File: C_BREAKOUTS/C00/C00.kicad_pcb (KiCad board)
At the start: 2 copper layers, 88.9 x 38.1 mm, 42 parts, among them J0 Conn_01x01_Male, J1 Conn_01x01_Male, J2 Conn_01x01_Male, J3 Conn_01x01_Male, J6 Conn_01x06_Female, J7 Conn_01x06_Female

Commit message: some comfort improvement
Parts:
- moved J0 20.3 mm to (49.2, 28.9)
- moved J1 20.3 mm to (49.2, 49.2)
- moved HZ3 1.30 mm to (91.3, 51.5)
- moved J7 0.40 mm to (97.0, 30.3)
- moved HZ0 0.40 mm to (23.4, 26.6)
- moved HZ1 0.40 mm to (23.4, 51.5)
- moved J6 0.30 mm to (104.9, 47.8)
- moved HZ2 0.30 mm to (92.3, 26.6)
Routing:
- net Net-(J6-Pad6): track 16.0 -> 0.00 mm
- net Net-(J6-Pad5): track 16.0 -> 0.00 mm
- net Net-(J6-Pad4): track 16.0 -> 0.00 mm
- net Net-(J6-Pad3): track 16.0 -> 0.00 mm
- net Net-(J6-Pad2): track 16.0 -> 0.00 mm
- net Net-(J6-Pad1): track 16.0 -> 0.00 mm
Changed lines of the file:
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@@
     (thickness 1.6)
     (drawings 8)
-    (tracks 15)
+    (tracks 0)
     (zones 0)
     (modules 42)
@@
   )
   (module TerminalBlock_4Ucon:TerminalBlock_4Ucon_1x06_P3.50mm_Horizontal (layer F.Cu)
-    (at 96.6 30.3 270)
+    (at 97 30.3 270)
     (descr "Terminal Block 4Ucon ItemNo. 19964, 6 pins, pitch 3.5mm, size 21.7x7mm^2, drill diamater 1.2mm, pad diameter 2.4mm, see http://www.4uconnector.com/online/object/4udrawing/19964.pdf, script-generated using https://github.com/pointhi/kicad-footprint-generator/scripts/TerminalBlock_4Ucon")
     (tags "THT Terminal Block 4Ucon ItemNo. 19964 pitch 3.5mm size 21.7x7mm^2 drill 1.2mm pad 2.4mm")
@@
   )
   (module TerminalBlock_4Ucon:TerminalBlock_4Ucon_1x06_P3.50mm_Horizontal (layer F.Cu)
-    (at 104.6 47.8 90)
+    (at 104.9 47.8 90)
     (descr "Terminal Block 4Ucon ItemNo. 19964, 6 pins, pitch 3.5mm, size 21.7x7mm^2, drill diamater 1.2mm, pad diameter 2.4mm, see http://www.4uconnector.com/online/object/4udrawing/19964.pdf, script-generated using https://github.com/pointhi/kicad-footprint-generator/scripts/TerminalBlock_4Ucon")
     (tags "THT Terminal Block 4Ucon ItemNo. 19964 pitch 3.5mm size 21.7x7mm^2 drill 1.2mm pad 2.4mm")
@@
   )
   (module Connector_Wire:SolderWirePad_1x01_Drill1mm (layer F.Cu)
-    (at 28.89 49.21)
+    (at 49.21 49.21)
     (descr "Wire solder connection")
     (tags connector)
@@
   )
   (module Connector_Wire:SolderWirePad_1x01_Drill1mm (layer F.Cu)
-    (at 28.89 28.89)
+    (at 49.21 28.89)
     (descr "Wire solder connection")
     (tags connector)
@@
   )
   (module MountingHole:MountingHole_3mm (layer F.Cu)
-    (at 92.56 51.55)
+    (at 91.26 51.55)
     (descr "Mounting Hole 3mm, no annular")
     (tags "mounting hole 3mm no annular")
@@
   )
   (module MountingHole:MountingHole_3mm (layer F.Cu)
-    (at 92.56 26.55)
+    (at 92.26 26.55)
     (descr "Mounting Hole 3mm, no annular")
     (tags "mounting hole 3mm no annular")
@@
   )
   (module MountingHole:MountingHole_3mm (layer F.Cu)
-    (at 23.81 51.55)
+    (at 23.41 51.55)
     (descr "Mounting Hole 3mm, no annular")
     (tags "mounting hole 3mm no annular")
@@
   )
   (module MountingHole:MountingHole_3mm (layer F.Cu)
-    (at 23.81 26.55)
+    (at 23.41 26.55)
     (descr "Mounting Hole 3mm, no annular")
     (tags "mounting hole 3mm no annular")
@@
     (effects (font (size 1.5 1.5) (thickness 0.3)))
   )
-  (gr_text C00_BREAKOUT (at 39.5224 29.0322 180) (layer B.SilkS)
+  (gr_text C00_BREAKOUT (at 37.5224 29.0322 180) (layer B.SilkS)
     (effects (font (size 1.5 1.5) (thickness 0.15)) (justify mirror))
   )
-  (gr_text C00_BREAKOUT (at 40.1574 49.3776) (layer F.SilkS)
+  (gr_text C00_BREAKOUT (at 38.1574 49.3776) (layer F.SilkS)
     (effects (font (size 1.5 1.5) (thickness 0.15)))
   )
@@
   (gr_line (start 20 20) (end 108.9 20) (layer Edge.Cuts) (width 0.05))
   (gr_line (start 20 20) (end 20 58.1) (layer Edge.Cuts) (width 0.05))
-  (segment (start 96.6 30.3) (end 104.6 30.3) (width 0.75) (layer F.Cu) (net 2))
-  (segment (start 96.6 30.3) (end 104.6 30.3) (width 0.75) (layer B.Cu) (net 2))
-  (segment (start 96.6 33.8) (end 104.6 33.8) (width 0.75) (layer F.Cu) (net 3))
-  (segment (start 96.6 33.8) (end 104.6 33.8) (width 0.75) (layer B.Cu) (net 3))
-  (segment (start 96.6 37.3) (end 104.6 37.3) (width 0.75) (layer F.Cu) (net 4))
-  (segment (start 98.297056 37.3) (end 104.6 37.3) (width 0.75) (layer B.Cu) (net 4))
-  (segment (start 96.6 37.3) (end 98.297056 37.3) (width 0.75) (layer B.Cu) (net 4))
-  (segment (start 96.6 40.8) (end 104.6 40.8) (width 0.75) (layer F.Cu) (net 5))
-  (segment (start 96.6 40.8) (end 104.6 40.8) (width 0.75) (layer B.Cu) (net 5))
-  (segment (start 98.297056 44.3) (end 104.6 44.3) (width 0.75) (layer F.Cu) (net 6))
-  (segment (start 96.6 44.3) (end 98.297056 44.3) (width 0.75) (layer F.Cu) (net 6))
-  (segment (start 96.6 44.3) (end 104.6 44.3) (width 0.75) (layer B.Cu) (net 6))
-  (segment (start 96.6 47.8) (end 104.6 47.8) (width 0.75) (layer F.Cu) (net 7))
-  (segment (start 98.297056 47.8) (end 104.6 47.8) (width 0.75) (layer B.Cu) (net 7))
-  (segment (start 96.6 47.8) (end 98.297056 47.8) (width 0.75) (layer B.Cu) (net 7))
   (zone (net 1) (net_name "Net-(J0-Pad1)") (layer F.Cu) (hatch edge 0.508)
     (connect_pads (clearance 0.508))
     (min_thickness 0.254)
-    (fill yes (arc_segments 32) (thermal_gap 0.508) (thermal_bridge_width 0.508))
+    (fill (arc_segments 32) (thermal_gap 0.508) (thermal_bridge_width 0.508))
     (polygon
       (pts
@@
     (connect_pads (clearance 0.508))
     (min_thickness 0.254)
-    (fill yes (arc_segments 32) (thermal_gap 0.508) (thermal_bridge_width 0.508))
+    (fill (arc_segments 32) (thermal_gap 0.508) (thermal_bridge_width 0.508))
     (polygon
       (pts

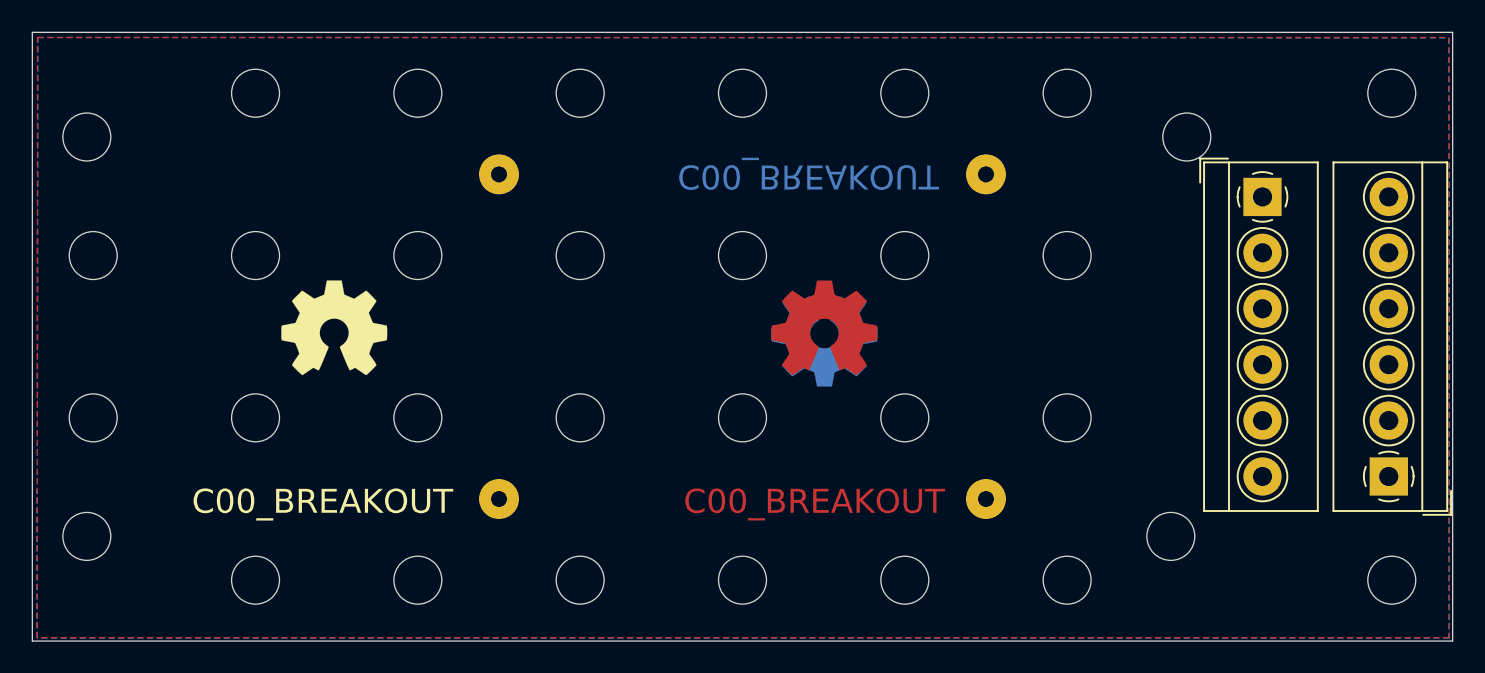
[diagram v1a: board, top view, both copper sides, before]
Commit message: more space, all traces routed
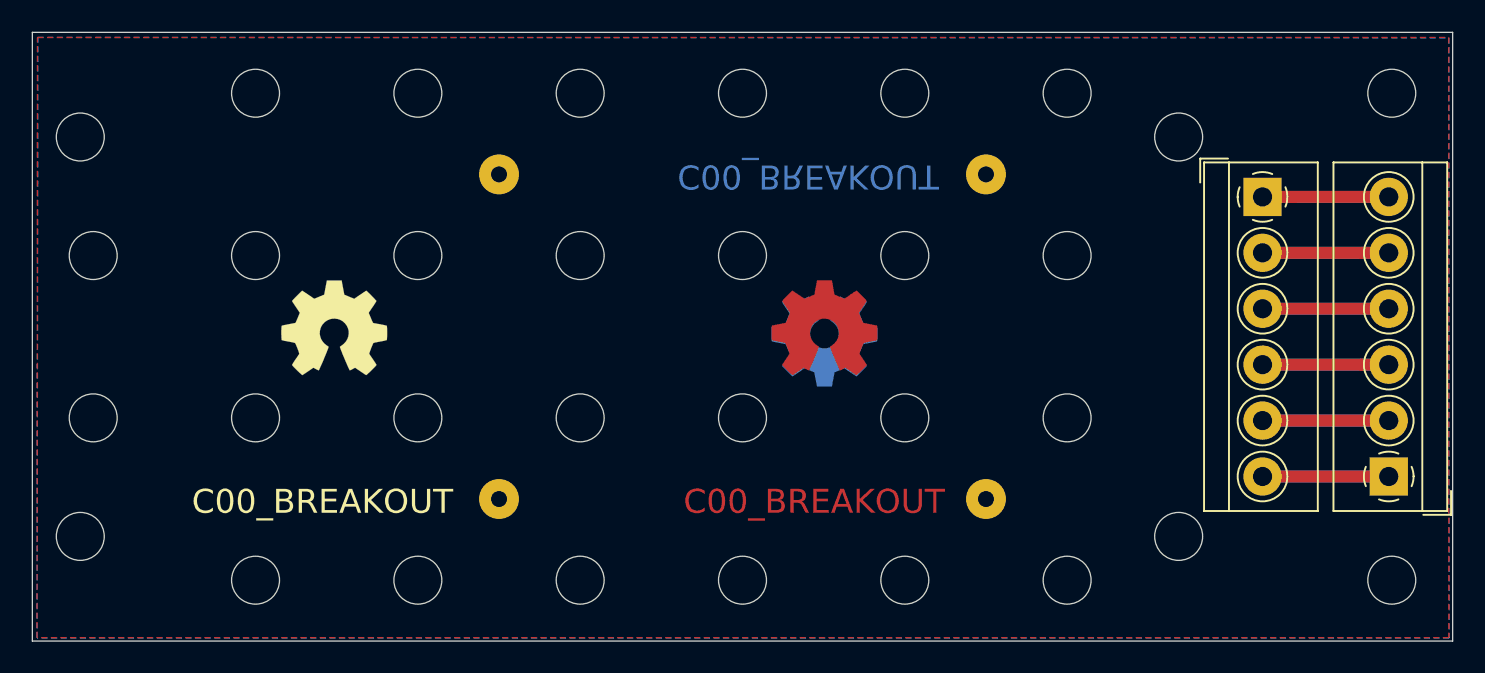
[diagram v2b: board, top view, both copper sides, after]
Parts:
- moved HZ2 0.51 mm to (91.8, 26.6)
- moved HZ3 0.49 mm to (91.8, 51.5)
- moved HZ0 0.41 mm to (23.0, 26.6)
- moved HZ1 0.41 mm to (23.0, 51.5)
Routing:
- net Net-(J6-Pad6): track 0.00 -> 15.8 mm
- net Net-(J6-Pad5): track 0.00 -> 15.8 mm
- net Net-(J6-Pad4): track 0.00 -> 15.8 mm
- net Net-(J6-Pad3): track 0.00 -> 15.8 mm
- net Net-(J6-Pad2): track 0.00 -> 15.8 mm
- net Net-(J6-Pad1): track 0.00 -> 15.8 mm
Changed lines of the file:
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@@
     (thickness 1.6)
     (drawings 8)
-    (tracks 0)
+    (tracks 16)
     (zones 0)
     (modules 42)
@@
   )
   (module MountingHole:MountingHole_3mm (layer F.Cu)
-    (at 91.26 51.55)
+    (at 91.75 51.55)
     (descr "Mounting Hole 3mm, no annular")
     (tags "mounting hole 3mm no annular")
@@
   )
   (module MountingHole:MountingHole_3mm (layer F.Cu)
-    (at 92.26 26.55)
+    (at 91.75 26.55)
     (descr "Mounting Hole 3mm, no annular")
     (tags "mounting hole 3mm no annular")
@@
   )
   (module MountingHole:MountingHole_3mm (layer F.Cu)
-    (at 23.41 51.55)
+    (at 23 51.55)
     (descr "Mounting Hole 3mm, no annular")
     (tags "mounting hole 3mm no annular")
@@
   )
   (module MountingHole:MountingHole_3mm (layer F.Cu)
-    (at 23.41 26.55)
+    (at 23 26.55)
     (descr "Mounting Hole 3mm, no annular")
     (tags "mounting hole 3mm no annular")
@@
   (gr_line (start 20 20) (end 108.9 20) (layer Edge.Cuts) (width 0.05))
   (gr_line (start 20 20) (end 20 58.1) (layer Edge.Cuts) (width 0.05))
+  (segment (start 98.95 30.3) (end 104.9 30.3) (width 0.75) (layer F.Cu) (net 2))
+  (segment (start 97 30.3) (end 98.95 30.3) (width 0.75) (layer F.Cu) (net 2))
+  (segment (start 98.95 30.3) (end 104.9 30.3) (width 0.75) (layer B.Cu) (net 2))
+  (segment (start 97 30.3) (end 98.95 30.3) (width 0.75) (layer B.Cu) (net 2))
+  (segment (start 103.202944 33.8) (end 97 33.8) (width 0.75) (layer F.Cu) (net 3))
+  (segment (start 104.9 33.8) (end 103.202944 33.8) (width 0.75) (layer F.Cu) (net 3))
+  (segment (start 104.9 33.8) (end 97 33.8) (width 0.75) (layer B.Cu) (net 3))
+  (segment (start 97 37.3) (end 104.9 37.3) (width 0.75) (layer F.Cu) (net 4))
+  (segment (start 97 37.3) (end 104.9 37.3) (width 0.75) (layer B.Cu) (net 4))
+  (segment (start 103.202944 40.8) (end 97 40.8) (width 0.75) (layer F.Cu) (net 5))
+  (segment (start 104.9 40.8) (end 103.202944 40.8) (width 0.75) (layer F.Cu) (net 5))
+  (segment (start 104.9 40.8) (end 97 40.8) (width 0.75) (layer B.Cu) (net 5))
+  (segment (start 97 44.3) (end 104.9 44.3) (width 0.75) (layer F.Cu) (net 6))
+  (segment (start 97 44.3) (end 104.9 44.3) (width 0.75) (layer B.Cu) (net 6))
+  (segment (start 104.9 47.8) (end 97 47.8) (width 0.75) (layer F.Cu) (net 7))
+  (segment (start 104.9 47.8) (end 97 47.8) (width 0.75) (layer B.Cu) (net 7))
   (zone (net 1) (net_name "Net-(J0-Pad1)") (layer F.Cu) (hatch edge 0.508)
     (connect_pads (clearance 0.508))
     (min_thickness 0.254)
-    (fill (arc_segments 32) (thermal_gap 0.508) (thermal_bridge_width 0.508))
+    (fill yes (arc_segments 32) (thermal_gap 0.508) (thermal_bridge_width 0.508))
     (polygon
       (pts
@@
     (connect_pads (clearance 0.508))
     (min_thickness 0.254)
-    (fill (arc_segments 32) (thermal_gap 0.508) (thermal_bridge_width 0.508))
+    (fill yes (arc_segments 32) (thermal_gap 0.508) (thermal_bridge_width 0.508))
     (polygon
       (pts
